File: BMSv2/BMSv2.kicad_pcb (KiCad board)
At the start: 2 copper layers, 126 parts, among them J1 Conn_01x05, J2 Conn_01x04_Socket, J3 Conn_01x02_Pin, J4 Conn_01x02_Pin, J5 Conn_01x03_Pin, Q1 AO3401A, Q10 MMBT3904, Q11 MMBT3904, Q12 MMBT3904, Q13 MMBT3904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

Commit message: Add files via upload
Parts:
- J1, J2, J3, J4, J5: moved to B.Cu
- moved Q17 17.0 mm to (97.1, 74.7), turned to 180 degrees
- moved J1 16.1 mm to (107.6, 74.5), turned to 90 degrees
- moved C27 14.5 mm to (99.8, 74.8), turned to 90 degrees
- moved J2 14.5 mm to (87.4, 81.1)
- moved R40 13.7 mm to (86.5, 75.7), turned to 180 degrees
- moved C24 12.4 mm to (103.7, 53.7)
- moved R45 12.2 mm to (96.9, 63.5)
- moved R34 12.0 mm to (104.0, 69.6), turned to 90 degrees
- moved R33 11.9 mm to (104.0, 65.2), turned to 90 degrees
- moved R36 11.9 mm to (104.0, 76.6), turned to 90 degrees
- moved R35 11.9 mm to (104.0, 73.2), turned to 90 degrees
- moved H1 11.8 mm to (109.7, 47.3)
- moved H2 11.8 mm to (109.6, 80.9)
- moved Q14 11.6 mm to (103.7, 56.3)
- moved Q10 11.2 mm to (100.6, 65.7)
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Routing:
- net Current: track 12.8 -> 0.00 mm
- net SWDCLK: track 12.1 -> 0.00 mm
- net CAN_STBY: track 11.6 -> 0.00 mm
- net UART_RX: track 11.3 -> 0.00 mm
- net SWDIO: track 10.9 -> 0.00 mm
- net CAN1_RX: track 10.7 -> 0.00 mm
- net UART_TX: track 10.5 -> 0.00 mm
- net CAN1_TX: track 9.75 -> 0.00 mm
- net CL4_DCH: track 7.24 -> 0.00 mm
- net CL1_DCH: track 6.96 -> 0.00 mm
- net CL3_DCH: track 6.77 -> 0.00 mm
- net CL2_DCH: track 6.51 -> 0.00 mm
- net Net-(Q13-B): track 6.68 -> 0.46 mm
- net Net-(Q10-B): track 5.74 -> 0.00 mm
- net Net-(Q12-B): track 5.60 -> 0.00 mm
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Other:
- board outline added: 44 x 41.2 mm
- board text added: "BOOT0"
- board text added: "CAN"
- board text added: "H"
- board text added: "L"
- board text added: "SWD"
- board text added: "UART"

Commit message: Rooting for power section
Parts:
- moved R46 2.83 mm to (83.9, 78.2)
- moved D6 2.23 mm to (87.0, 78.3)
- moved R29 1.82 mm to (96.3, 66.3)
- moved R30 1.82 mm to (96.3, 68.3)
- moved R31 1.82 mm to (96.2, 70.3)
- moved R32 1.82 mm to (96.3, 72.2)
- moved F1 1.77 mm to (81.0, 55.8)
- moved R6 1.75 mm to (93.7, 47.1)
- moved D1 1.23 mm to (78.7, 52.5)
- moved C16 1.20 mm to (90.2, 50.4), turned to 0 degrees
- moved R9 1.03 mm to (86.5, 50.7)
- moved C15 0.76 mm to (90.2, 47.4)
- moved R8 0.64 mm to (85.4, 50.7)
- moved C21 0.58 mm to (83.4, 47.6)
- moved C13 0.53 mm to (80.8, 52.4)
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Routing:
- net VIN: track 0.00 -> 17.2 mm
- net +12V: track 0.00 -> 17.1 mm
- net Net-(U4-SW): track 0.00 -> 8.32 mm
- net Net-(C17-Pad2): track 0.00 -> 5.50 mm
- net Net-(C13-Pad1): track 0.00 -> 3.86 mm, vias 0 -> 2
- net Net-(Q1-S): track 0.00 -> 3.67 mm
- net Net-(U4-EN): track 3.83 -> 5.60 mm
- net Net-(C16-Pad2): track 0.00 -> 1.38 mm
- net Net-(U4-FB): track 0.90 -> 2.24 mm, vias 0 -> 2
- net Net-(U4-SS): track 2.31 -> 1.44 mm
- net GND: vias 0 -> 6
- net (no net): vias 0 -> 6
- added copper zone on F.Cu, net +3.3V
- added copper zone on F.Cu, net +5V
- added copper zone on F.Cu, net GND
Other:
- board text added: "STM32F405RGTx"

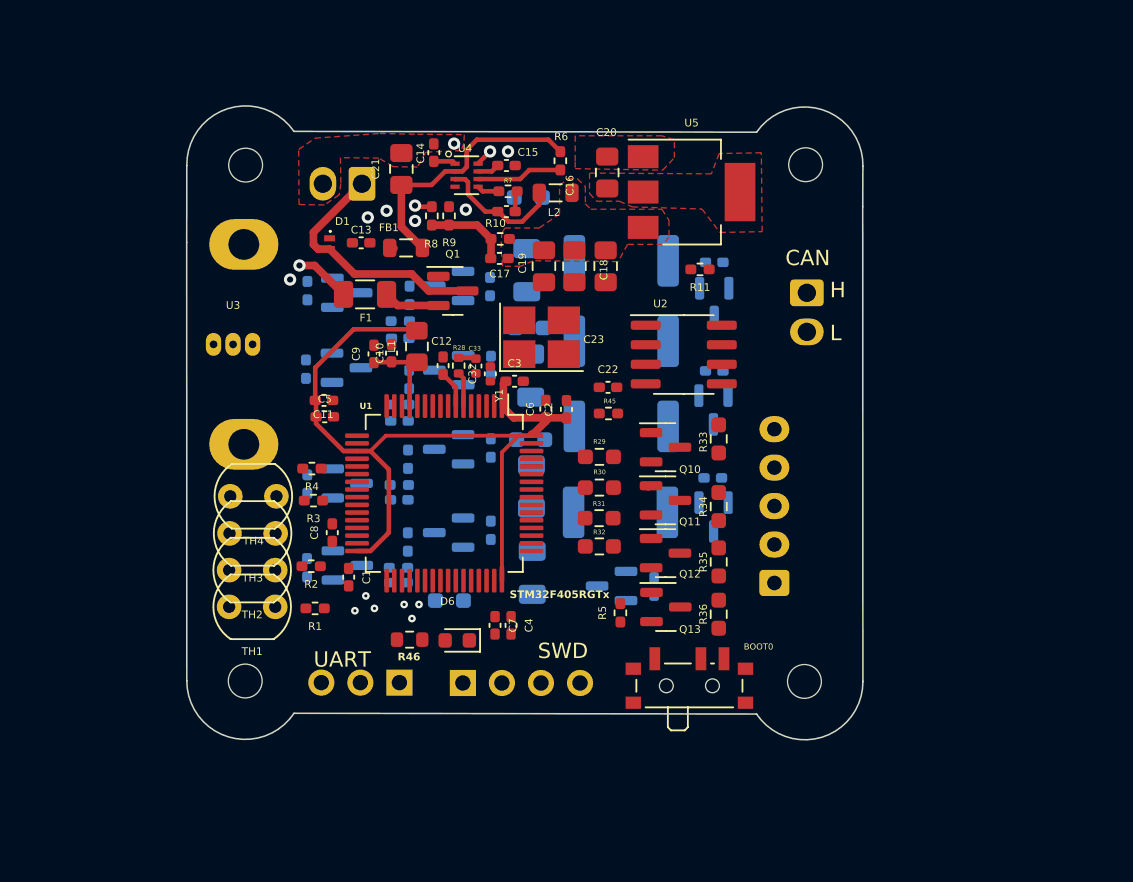
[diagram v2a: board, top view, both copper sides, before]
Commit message: Added for Front flayer
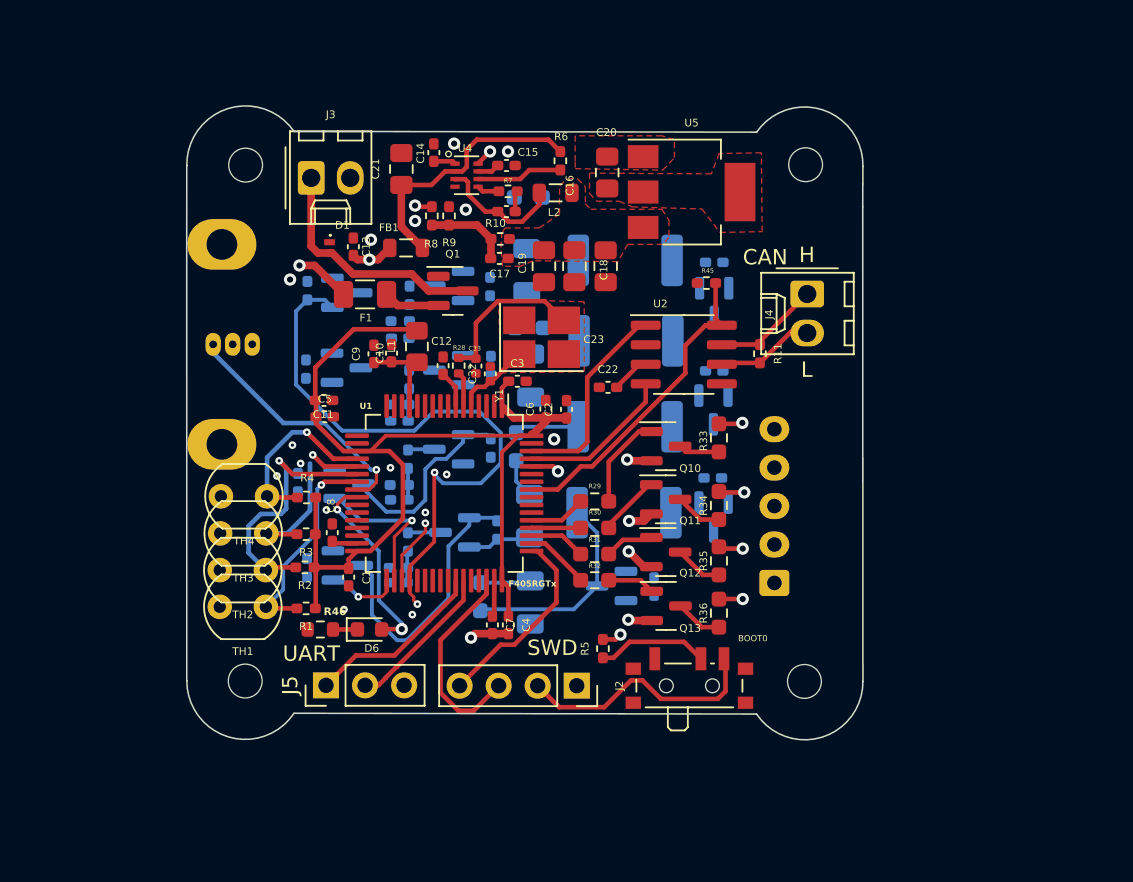
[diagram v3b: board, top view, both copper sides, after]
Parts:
- J2, J3, J4, J5: moved to F.Cu
- U3: moved to B.Cu
- moved R45 10.6 mm to (103.2, 55.0)
- moved J2 7.41 mm to (94.8, 81.2)
- moved R11 6.73 mm to (106.7, 59.6), turned to -90 degrees
- moved R46 5.84 mm to (78.1, 77.6)
- moved D6 5.75 mm to (81.3, 77.6), turned to 0 degrees
- moved J5 4.78 mm to (78.5, 81.2)
- moved J3 3.32 mm to (77.5, 48.2), turned to 0 degrees
- moved R29 2.91 mm to (96.0, 69.2)
- moved R30 2.64 mm to (96.0, 71.0)
- moved R5 2.59 mm to (96.5, 78.8)
- moved R31 2.35 mm to (96.0, 72.7)
- moved R3 2.24 mm to (77.2, 71.4)
- moved R32 2.22 mm to (96.0, 74.4)
- moved R40 2.02 mm to (88.5, 75.4), turned to -90 degrees
- moved D4 1.93 mm to (91.7, 70.2)
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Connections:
- J2 pad 1: SWDCLK -> GND
- J2 pad 2: SWDIO -> +3.3V
- J2 pad 3: +3.3V -> SWDIO
- J2 pad 4: GND -> SWDCLK
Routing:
- net CELL4_M_TRIG: track 0.00 -> 39.9 mm, vias 0 -> 2
- net +3.3V: track 54.0 -> 85.3 mm
- net CAN_STBY: track 0.00 -> 20.8 mm
- net Net-(Q8-C): track 0.00 -> 18.0 mm
- net Temp2: track 0.00 -> 17.2 mm, vias 0 -> 1
- net Current: track 0.00 -> 17.1 mm, vias 0 -> 1
- net Temp1: track 0.00 -> 14.2 mm, vias 0 -> 1
- net Net-(Q17-C): track 0.00 -> 13.6 mm
- net SWDIO: track 0.00 -> 13.5 mm
- net CAN1_TX: track 0.00 -> 13.3 mm
- net Net-(Q6-C): track 0.00 -> 12.9 mm
- net SWDCLK: track 0.00 -> 12.8 mm
- net LED_STATUS: track 0.00 -> 12.7 mm, vias 0 -> 2
- net Temp3: track 0.00 -> 12.0 mm, vias 0 -> 1
- net Temp4: track 0.00 -> 11.9 mm, vias 0 -> 1
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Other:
- board text added: "F405RGTx"
- board text removed: "STM32F405RGTx"

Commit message: fast commit
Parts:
- moved R44 5.72 mm to (98.1, 75.7)
- moved C24 2.46 mm to (103.0, 56.0), turned to 90 degrees
- moved Q14 1.93 mm to (105.4, 55.3), turned to 90 degrees
- moved R37 1.34 mm to (92.3, 50.7)
- moved R39 0.63 mm to (91.5, 65.7)
- moved Q16 0.58 mm to (103.7, 70.8)
- moved C26 0.58 mm to (103.6, 68.3)
- moved C25 0.40 mm to (103.7, 61.2)
- moved Q15 0.40 mm to (103.7, 63.7)
- moved R12 0.31 mm to (89.2, 55.6)
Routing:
- net CELL2: track 0.00 -> 51.1 mm
- net CELL4: track 0.00 -> 31.3 mm
- net CELL1: track 4.16 -> 31.5 mm
- net Net-(Q14-B): track 1.55 -> 10.9 mm
- net Net-(Q4-C): track 0.00 -> 8.81 mm
- net Net-(Q17-B): track 1.55 -> 10.1 mm
- net Net-(Q2-C): track 0.00 -> 7.20 mm
- net Net-(Q16-C): track 4.20 -> 0.00 mm
- net Net-(Q15-C): track 0.00 -> 2.68 mm
- net Net-(D4-A): track 2.56 -> 0.00 mm
- net Net-(D2-A): track 0.00 -> 2.21 mm
- net CELL4_M: track 0.00 -> 2.21 mm
- net CELL4_M_TRIG: track 39.9 -> 38.0 mm
- net CELL1_M_TRIG: track 4.81 -> 6.57 mm
- net CELL3: track 0.00 -> 1.74 mm
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
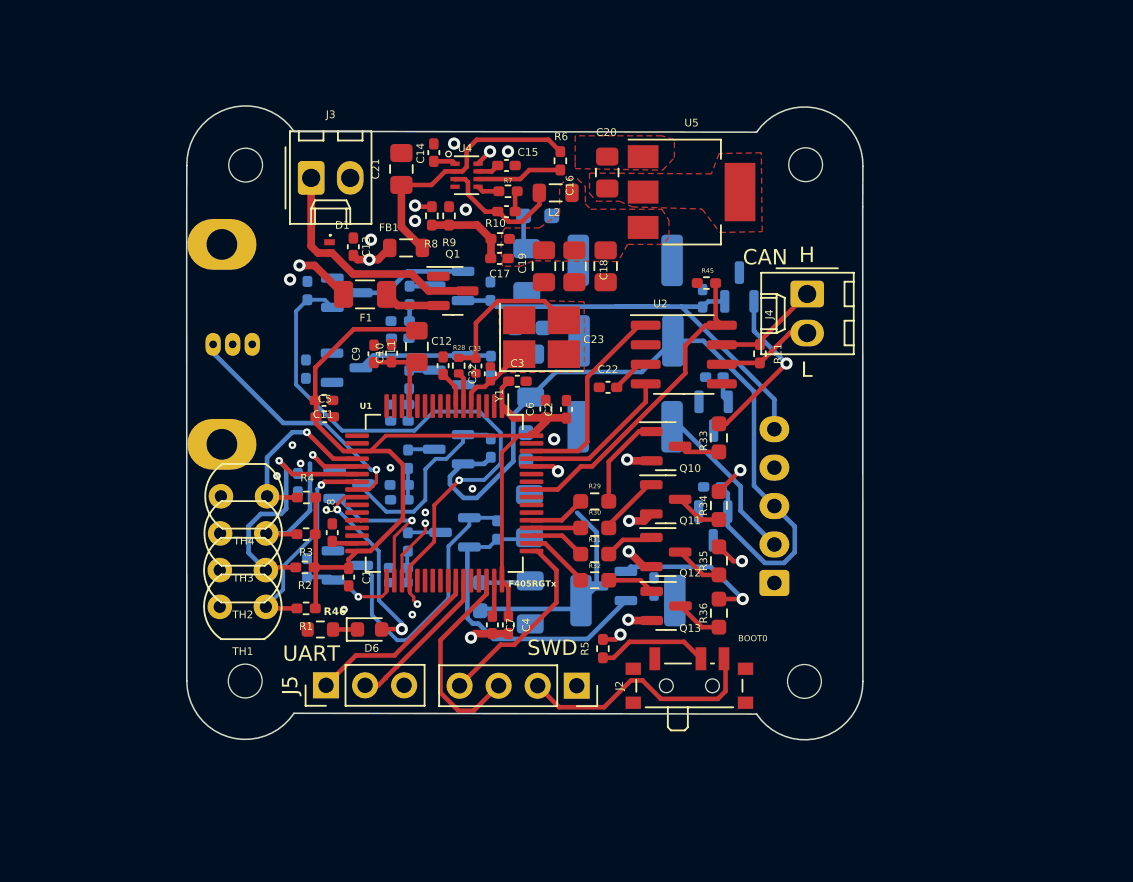
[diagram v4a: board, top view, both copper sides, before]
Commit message: Solving DRC Errors
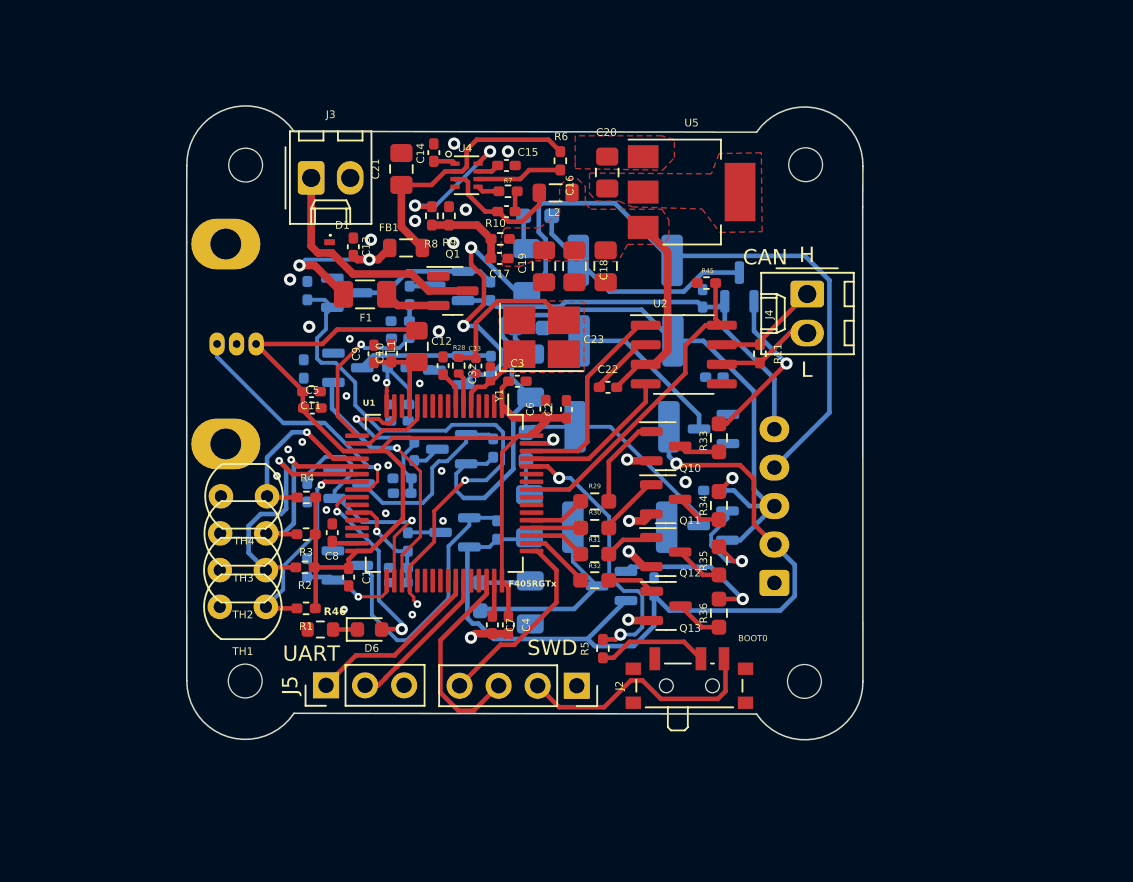
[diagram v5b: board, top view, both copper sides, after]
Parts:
- moved R44 4.80 mm to (97.6, 70.9)
- moved R16 1.13 mm to (83.1, 60.5), turned to 180 degrees
- moved C11 0.99 mm to (77.5, 62.1)
- moved C5 0.99 mm to (77.6, 63.2)
- moved R26 0.90 mm to (77.3, 68.7), turned to -90 degrees
- moved Q15 0.83 mm to (103.7, 64.5), turned to 180 degrees
- moved R19 0.65 mm to (84.2, 66.0), turned to 90 degrees
- moved C30 0.47 mm to (83.4, 68.7)
- moved R20 0.47 mm to (83.4, 67.7)
- moved U3 0.26 mm to (72.7, 59.0)
- moved C26 0.23 mm to (103.6, 68.5)
- moved Q7 0.21 mm to (86.7, 65.8)
- moved R43 0.20 mm to (97.7, 64.4)
- moved R18 0.15 mm to (89.4, 65.8)
- moved R25 0.14 mm to (77.0, 60.6)
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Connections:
- U1 pad 14: CELL1_M -> unconnected-(U1-PA0-Pad14)
- U1 pad 27: unconnected-(U1-PB1-Pad27) -> CELL1_M
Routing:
- net CELL3: track 1.74 -> 59.1 mm, vias 0 -> 2
- net CELL1: track 31.5 -> 54.5 mm, vias 0 -> 1
- net Net-(Q14-C): track 1.17 -> 16.6 mm
- net Net-(U1-BOOT0): track 3.13 -> 17.9 mm
- net Net-(Q16-C): track 0.00 -> 14.4 mm
- net CELL3_M_TRIG: track 4.36 -> 16.7 mm
- net GND: track 9.20 -> 20.4 mm, vias 20 -> 30
- net CELL2_M: track 2.05 -> 12.9 mm, vias 0 -> 1
- net Net-(Q15-C): track 2.68 -> 13.4 mm
- net CELL4_M: track 2.21 -> 12.8 mm, vias 0 -> 1
- net +5V: track 2.52 -> 13.0 mm
- net CELL2_M_TRIG: track 10.1 -> 16.9 mm
- net Net-(U4-FB): track 2.24 -> 8.58 mm
- net +3.3V: track 85.3 -> 91.1 mm
- net Net-(Q16-B): track 1.88 -> 6.99 mm
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
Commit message: GND connected
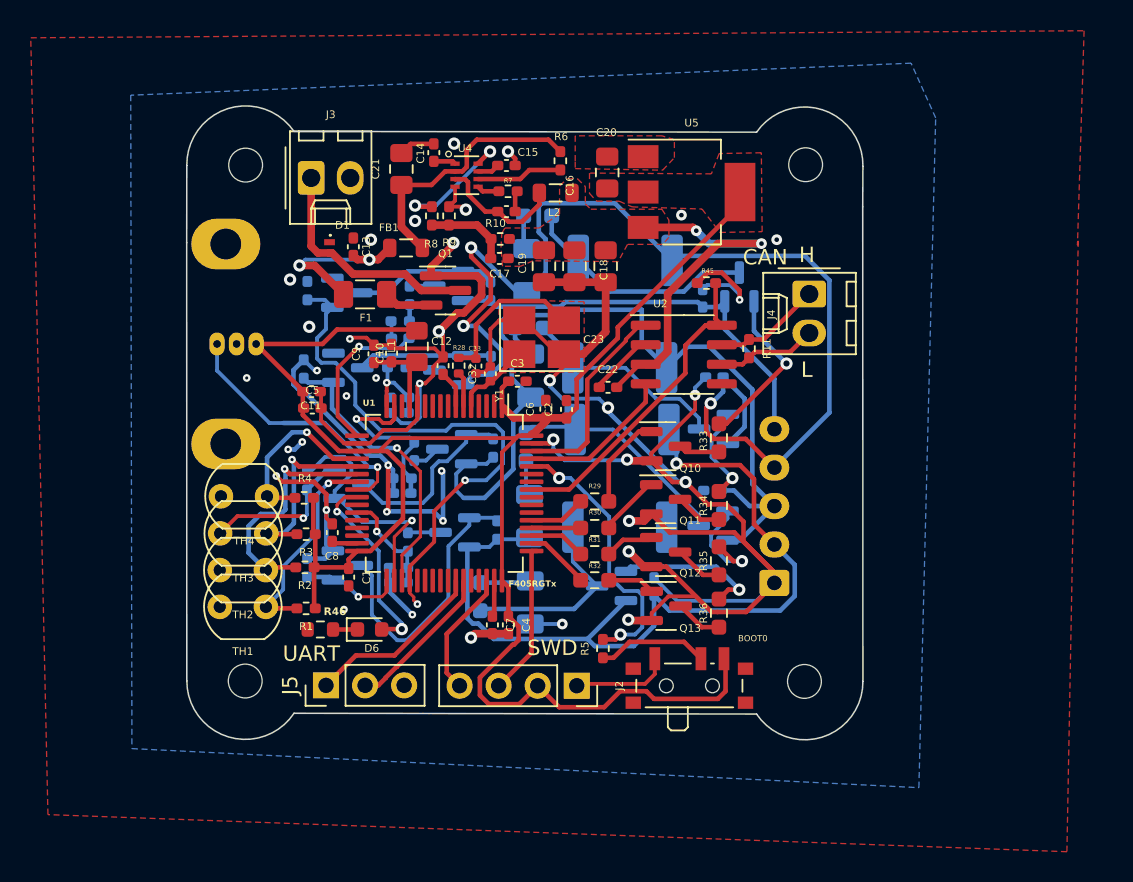
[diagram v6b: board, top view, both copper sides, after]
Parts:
- moved R42 1.80 mm to (97.6, 60.6)
- moved R26 0.79 mm to (77.2, 67.9)
- moved R11 0.78 mm to (106.0, 59.3)
- moved C29 0.53 mm to (83.3, 63.5)
- moved Q1 0.47 mm to (86.3, 55.5)
- moved R17 0.46 mm to (83.3, 62.5)
- moved R43 0.18 mm to (97.7, 64.6)
- moved R4 0.15 mm to (77.1, 69.0)
- moved J4 0.13 mm to (109.9, 55.8)
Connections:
- J2 pad 3: SWDIO -> SWDCLK
- J2 pad 4: SWDCLK -> SWDIO
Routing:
- net GND: track 20.4 -> 218.7 mm, vias 30 -> 40
- net +3.3V: track 91.1 -> 120.7 mm
- net CELL3: track 59.1 -> 74.3 mm, vias 2 -> 3
- net +5V: track 13.0 -> 24.0 mm, vias 0 -> 2
- net SWDIO: track 13.5 -> 8.26 mm
- net Net-(Q15-B): track 1.24 -> 6.38 mm
- net SWDCLK: track 12.8 -> 10.0 mm
- net CELL2: track 54.4 -> 56.9 mm
- net CELL3_M_TRIG: track 16.7 -> 18.8 mm
- net Temp2: track 17.2 -> 15.9 mm
- net CAN1-: track 7.43 -> 6.65 mm
- net CELL2_M_TRIG: track 16.9 -> 16.3 mm
- net Current: track 16.7 -> 17.3 mm
- added copper zone on B.Cu, net GND

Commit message: DRC Errors deletion
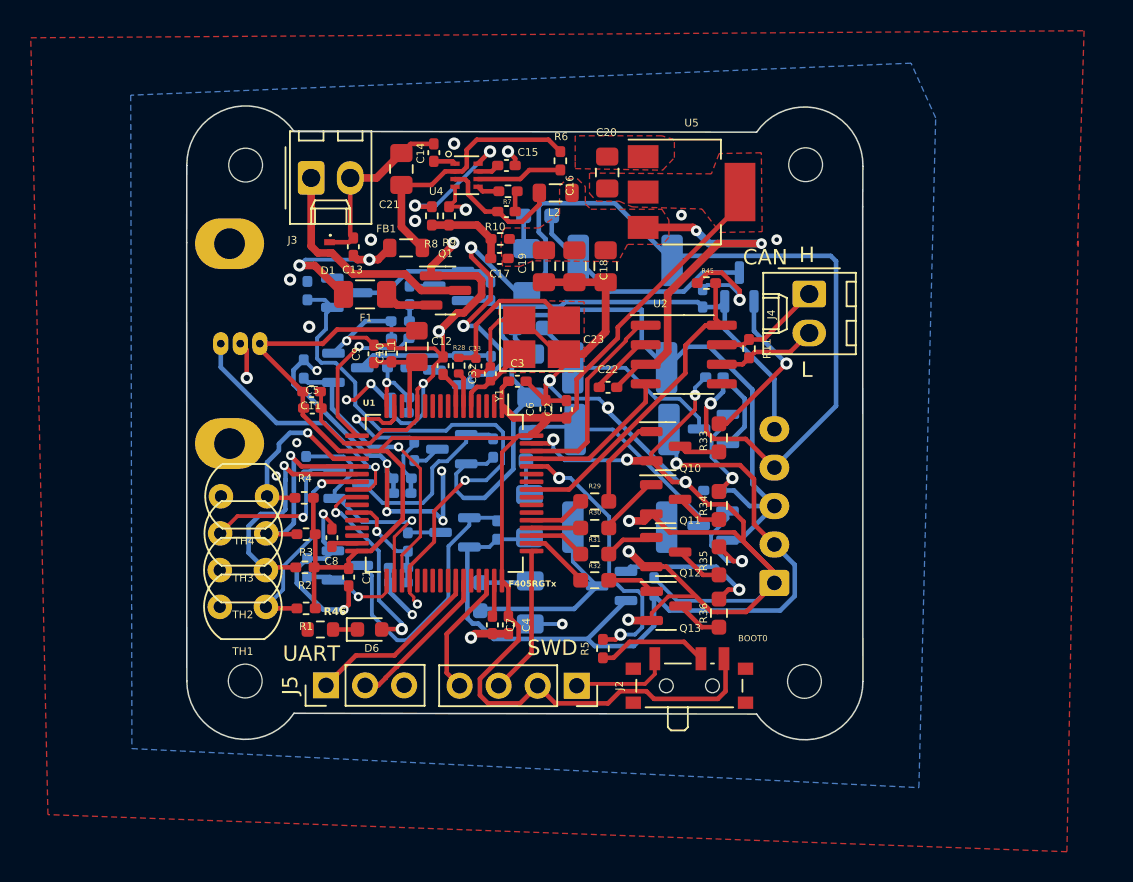
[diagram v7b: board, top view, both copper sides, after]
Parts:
- moved R26 0.98 mm to (77.2, 66.9)
- moved C8 0.33 mm to (78.9, 71.6)
- moved U3 0.24 mm to (72.9, 59.0)
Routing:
- net GND: track 218.7 -> 246.5 mm, vias 40 -> 39
- net CELL3: track 74.3 -> 75.6 mm
- net +3.3V: track 120.7 -> 120.2 mm
- net Current: track 17.3 -> 16.7 mm
- net Temp3: track 12.9 -> 13.4 mm
